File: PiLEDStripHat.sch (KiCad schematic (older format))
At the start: 8 parts, among them CON1 BARREL_JACK, J1 RPi_GPIO, P1 CONN_01X04, P2 CONN_01X02, U1 74AHC125

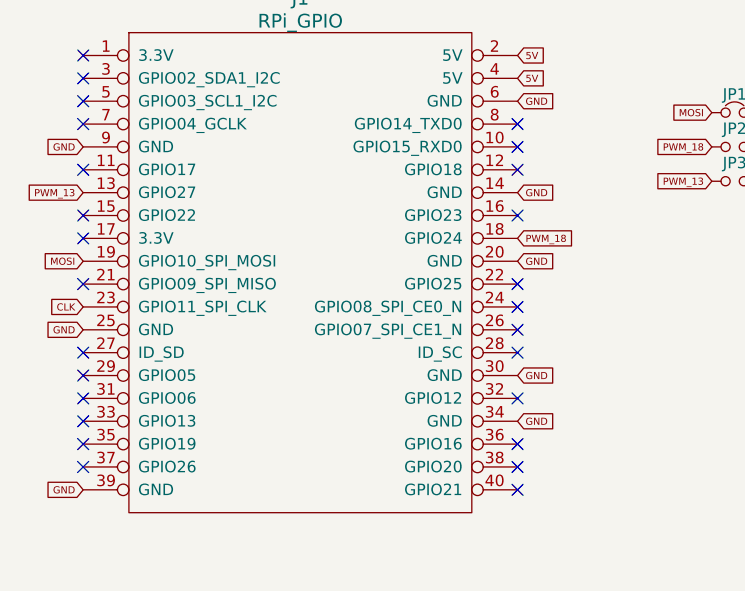
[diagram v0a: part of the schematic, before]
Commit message: fixed GPIO mappings
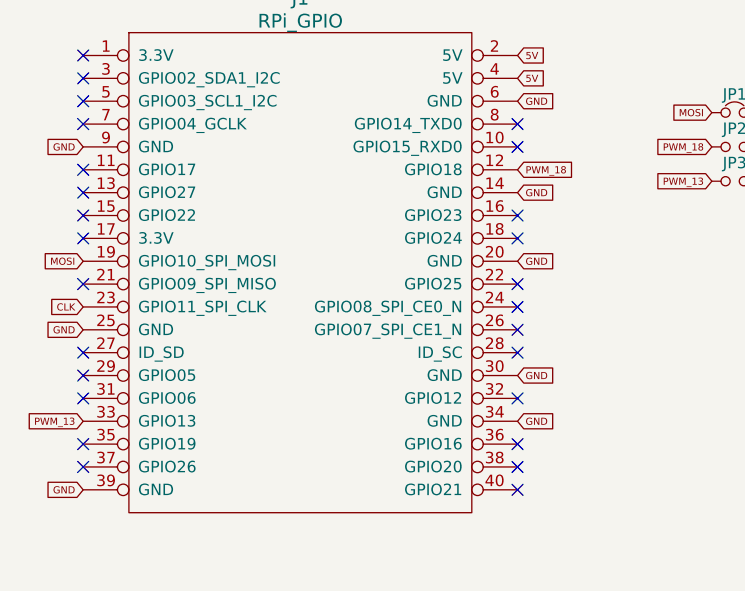
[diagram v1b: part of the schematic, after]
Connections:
- net PWM_13: now also J1.33 (GPIO13); no longer J1.13 (GPIO27)
- net PWM_18: now also J1.12 (GPIO18); no longer J1.18 (GPIO24)
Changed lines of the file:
@@
 Text GLabel 4800 3400 0    31   Input ~ 0
 MOSI
-Text GLabel 6700 3300 2    31   Input ~ 0
+Text GLabel 6700 3000 2    31   Input ~ 0
 PWM_18
-Text GLabel 4800 3100 0    31   Input ~ 0
+Text GLabel 4800 4100 0    31   Input ~ 0
 PWM_13
 $Comp
@@
 NoConn ~ 6700 2800
 NoConn ~ 6700 2900
-NoConn ~ 6700 3000
 NoConn ~ 6700 3200
 NoConn ~ 6700 3500
@@
 NoConn ~ 4800 3900
 NoConn ~ 4800 4000
-NoConn ~ 4800 4100
 NoConn ~ 4800 4200
 NoConn ~ 4800 4300
@@
 NoConn ~ 6700 4000
 NoConn ~ 6700 4200
+NoConn ~ 6700 3300
+NoConn ~ 4800 3100
 $EndSCHEMATC
